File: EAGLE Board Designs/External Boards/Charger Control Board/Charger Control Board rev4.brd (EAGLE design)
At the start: 81 parts

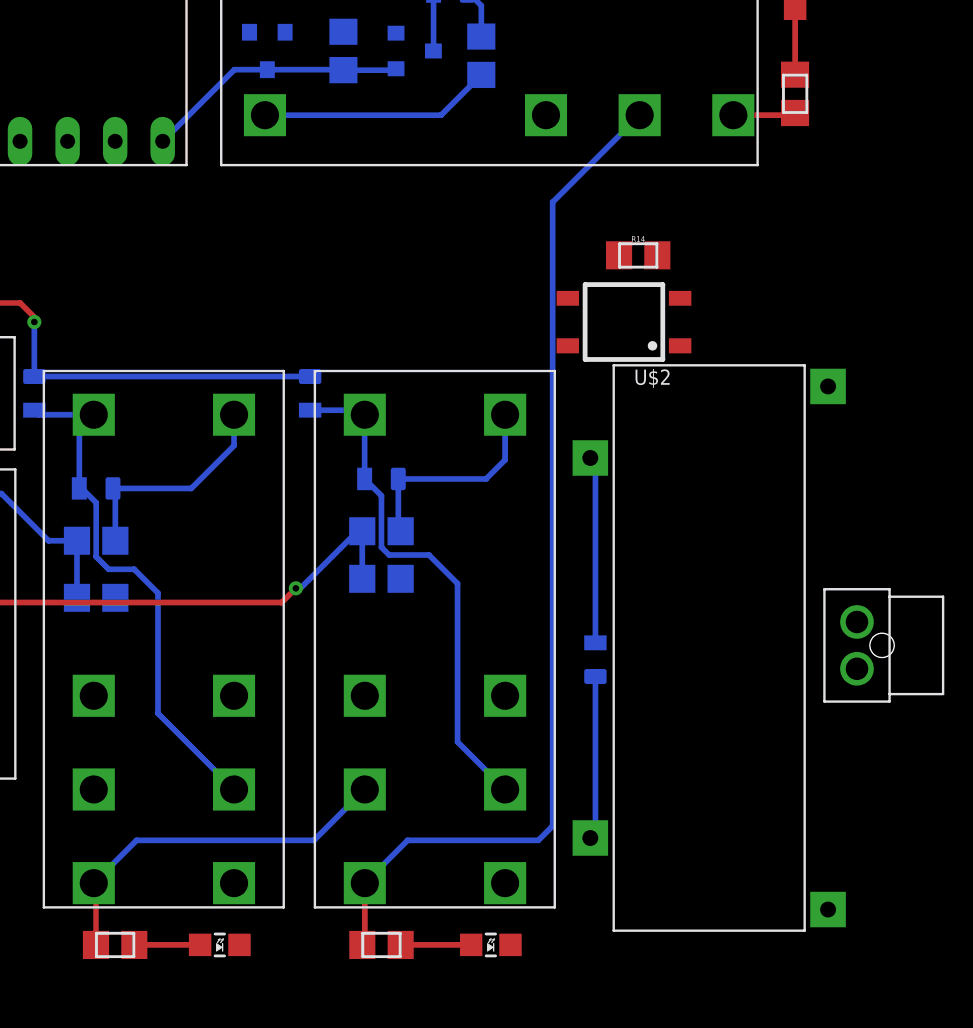
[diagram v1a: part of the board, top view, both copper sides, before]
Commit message: Routed charger
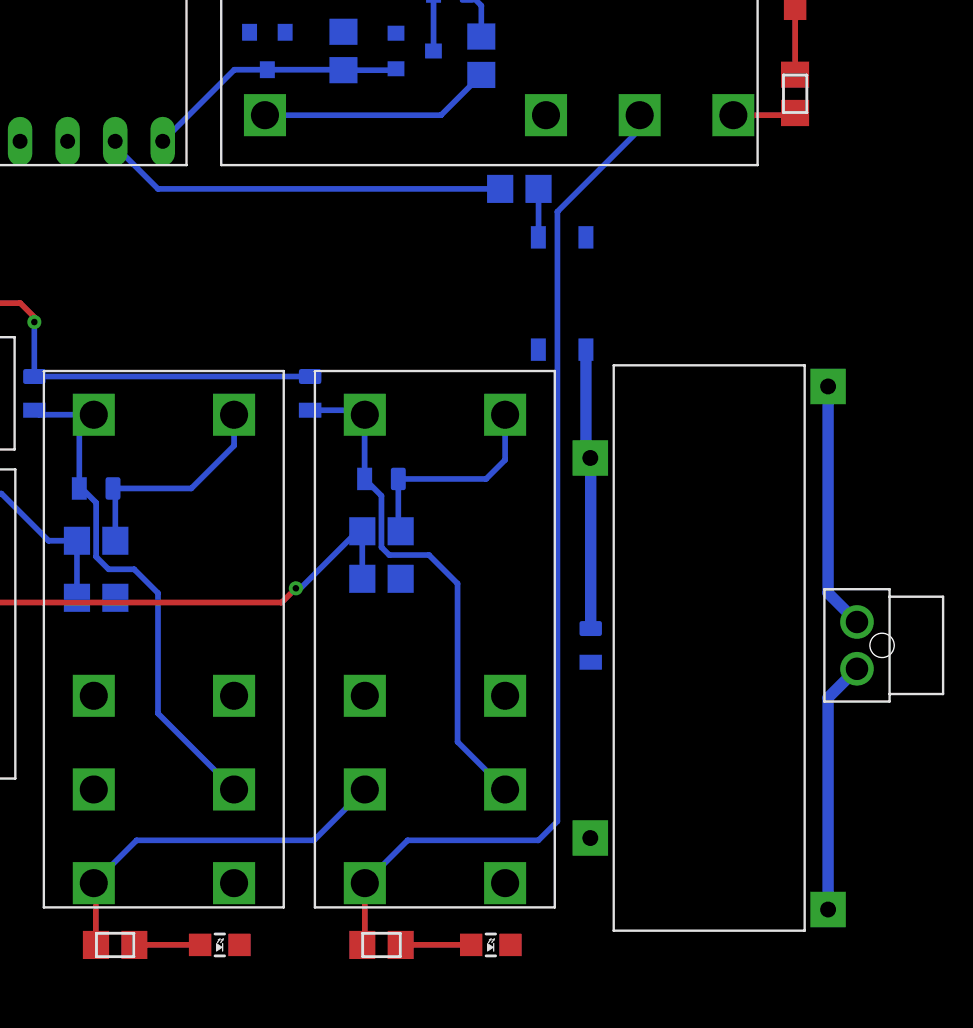
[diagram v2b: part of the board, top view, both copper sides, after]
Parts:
- moved R14 7.28 mm to (-24.1, 63.2), flipped to the bottom, turned to 180 degrees
- moved U$2 3.64 mm to (-21.8, 57.7), flipped to the bottom, turned to 180 degrees
- moved D3 0.80 mm to (-20.3, 38.9), turned to 90 degrees
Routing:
- net TOGGLE_CHARGER: track 0.00 -> 21.8 mm
- net CHARGER_1: track 0.00 -> 13.4 mm
- net CHARGER_2: track 0.00 -> 13.1 mm
- net GND: track 9.60 -> 0.00 mm
- net CHARGE_CONTROL: track 8.35 -> 15.1 mm
- net N$10: track 0.00 -> 2.59 mm
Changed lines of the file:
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@@
 <attribute name="VALUE" x="-36.0172" y="52.324" size="0.3048" layer="28" rot="MR90" align="top-center"/>
 </element>
-<element name="D3" library="HyTechDevices" package="0805_D" value="DIODE" x="-20.066" y="38.1" smashed="yes" rot="MR270">
-<attribute name="NAME" x="-20.7899" y="38.1" size="0.3048" layer="26" rot="MR270" align="bottom-center"/>
-<attribute name="VALUE" x="-19.3548" y="38.1" size="0.3048" layer="28" rot="MR270" align="top-center"/>
+<element name="D3" library="HyTechDevices" package="0805_D" value="DIODE" x="-20.32" y="38.862" smashed="yes" rot="MR90">
+<attribute name="NAME" x="-19.5961" y="38.862" size="0.3048" layer="26" rot="MR90" align="bottom-center"/>
+<attribute name="VALUE" x="-21.0312" y="38.862" size="0.3048" layer="28" rot="MR90" align="top-center"/>
 </element>
 <element name="D6" library="HyTechDevices" package="0805_D" value="TS4148 RYG" x="-31.496" y="47.752" smashed="yes" rot="MR180">
@@
 <attribute name="VALUE" x="-65.786" y="50.3428" size="0.3048" layer="27" align="top-center"/>
 </element>
-<element name="R14" library="HyTechDevices" package="0805" value="360" x="-17.78" y="59.69" smashed="yes">
-<attribute name="NAME" x="-17.78" y="60.4139" size="0.3048" layer="25" align="bottom-center"/>
-<attribute name="TOLERANCE" value="1%" x="-17.78" y="59.69" size="1.778" layer="27" display="off"/>
-<attribute name="VALUE" x="-17.78" y="58.9788" size="0.3048" layer="27" align="top-center"/>
+<element name="R14" library="HyTechDevices" package="0805" value="360" x="-24.13" y="63.246" smashed="yes" rot="MR180">
+<attribute name="NAME" x="-24.13" y="62.5221" size="0.3048" layer="26" rot="MR180" align="bottom-center"/>
+<attribute name="TOLERANCE" value="1%" x="-24.13" y="63.246" size="1.778" layer="28" rot="MR180" display="off"/>
+<attribute name="VALUE" x="-24.13" y="63.9572" size="0.3048" layer="28" rot="MR180" align="top-center"/>
 </element>
 <element name="R15" library="HyTechDevices" package="0805" value="68" x="71.12" y="69.85" smashed="yes" rot="R90">
@@
 <attribute name="VALUE" x="-75.311" y="57.531" size="0.3048" layer="28" rot="MR0" align="bottom-center"/>
 </element>
-<element name="U$2" library="HyTechDevices" package="SOP04" value="CPC1002N" x="-18.542" y="56.134" smashed="yes" rot="R90">
-<attribute name="NAME" x="-16.002" y="53.594" size="0.8128" layer="25" rot="R180"/>
-<attribute name="VALUE" x="-16.002" y="59.944" size="1.27" layer="27" rot="R180"/>
+<element name="U$2" library="HyTechDevices" package="SOP04" value="CPC1002N" x="-21.844" y="57.658" smashed="yes" rot="MR180">
+<attribute name="NAME" x="-24.384" y="60.198" size="0.8128" layer="26" rot="MR270"/>
+<attribute name="VALUE" x="-18.034" y="60.198" size="1.27" layer="28" rot="MR270"/>
 </element>
 <element name="U$4" library="HyTechDevices" package="TEENSY_3.2_SIMPLE" value="TEENSY_3.2_SIMPLE" x="-41.91" y="64.516" smashed="yes" rot="R90"/>
@@
 <contactref element="R29" pad="2"/>
 <contactref element="R31" pad="2"/>
-<wire x1="-20.066" y1="39" x2="-20.066" y2="48.598" width="0.3048" layer="16"/>
 <contactref element="U$3" pad="C1"/>
 <wire x1="68.58" y1="78.52" x2="78.74" y2="78.52" width="0" layer="19" extent="1-1"/>
@@
 <wire x1="54.61" y1="68.335" x2="59.69" y2="68.335" width="0" layer="19" extent="1-1"/>
 <wire x1="-9.398" y1="74.964" x2="54.61" y2="68.335" width="0" layer="19" extent="1-1"/>
-<wire x1="-15.542" y1="57.404" x2="-9.398" y2="74.964" width="0" layer="19" extent="1-1"/>
-<wire x1="-20.066" y1="48.598" x2="-15.542" y2="57.404" width="0" layer="19" extent="1-16"/>
-<wire x1="-20.34" y1="28.572" x2="-20.066" y2="39" width="0" layer="19" extent="16-16"/>
+<wire x1="-20.574" y1="60.658" x2="-9.398" y2="74.964" width="0" layer="19" extent="1-1"/>
+<wire x1="-20.32" y1="37.962" x2="-20.574" y2="60.658" width="0" layer="19" extent="1-16"/>
+<wire x1="-20.32" y1="37.962" x2="-20.34" y2="28.572" width="0" layer="19" extent="16-16"/>
 <wire x1="-24.892" y1="26.162" x2="-20.34" y2="28.572" width="0" layer="19" extent="1-1"/>
 <wire x1="-24.604" y1="22.86" x2="-24.892" y2="26.162" width="0" layer="19" extent="1-1"/>
-<wire x1="-30.471" y1="42.418" x2="-20.066" y2="39" width="0" layer="19" extent="16-16"/>
+<wire x1="-30.471" y1="42.418" x2="-20.32" y2="37.962" width="0" layer="19" extent="16-16"/>
 <wire x1="-39.082" y1="22.86" x2="-24.604" y2="22.86" width="0" layer="19" extent="1-1"/>
 <wire x1="-39.37" y1="26.162" x2="-39.082" y2="22.86" width="0" layer="19" extent="1-1"/>
@@
 <contactref element="U$2" pad="1"/>
 <contactref element="R14" pad="2"/>
-<wire x1="-15.542" y1="54.864" x2="-16.755" y2="59.69" width="0" layer="19" extent="1-1"/>
+<wire x1="-23.105" y1="63.246" x2="-23.105" y2="60.667" width="0.3048" layer="16"/>
+<wire x1="-23.105" y1="60.667" x2="-23.114" y2="60.658" width="0.3048" layer="16"/>
 </signal>
 <signal name="TOGGLE_CHARGER">
 <contactref element="R14" pad="1"/>
 <contactref element="U$4" pad="D11"/>
-<wire x1="-45.72" y1="65.786" x2="-18.805" y2="59.69" width="0" layer="19" extent="1-1"/>
+<wire x1="-25.155" y1="63.246" x2="-43.434" y2="63.246" width="0.3048" layer="16"/>
+<wire x1="-43.434" y1="63.246" x2="-45.72" y2="65.532" width="0.3048" layer="16"/>
+<wire x1="-45.72" y1="65.532" x2="-45.72" y2="65.786" width="0.3048" layer="16"/>
 </signal>
 <signal name="CHARGE_CONTROL">
 <contactref element="U$2" pad="3"/>
 <contactref element="D3" pad="C"/>
-<wire x1="-20.066" y1="37.2" x2="-20.066" y2="28.846" width="0.3048" layer="16"/>
 <contactref element="U$3" pad="C2"/>
-<wire x1="-20.34" y1="48.872" x2="-21.542" y2="57.404" width="0" layer="19" extent="1-1"/>
-<wire x1="-20.066" y1="37.2" x2="-20.34" y2="48.872" width="0" layer="19" extent="16-16"/>
+<wire x1="-20.32" y1="39.762" x2="-20.34" y2="39.782" width="0.3048" layer="16"/>
+<wire x1="-20.405" y1="48.937" x2="-20.34" y2="48.872" width="0.3048" layer="16"/>
+<wire x1="-20.574" y1="54.658" x2="-20.574" y2="49.106" width="0.6096" layer="16"/>
+<wire x1="-20.574" y1="49.106" x2="-20.405" y2="48.937" width="0.6096" layer="16"/>
+<wire x1="-20.32" y1="39.762" x2="-20.32" y2="48.852" width="0.6096" layer="16"/>
+<wire x1="-20.32" y1="48.852" x2="-20.405" y2="48.937" width="0.6096" layer="16"/>
 </signal>
 <signal name="+5V">
@@
 <wire x1="-26.162" y1="73.036" x2="-26.162" y2="71.383" width="0.3048" layer="16"/>
 <wire x1="-26.913" y1="73.787" x2="-10.16" y2="136.915" width="0" layer="19" extent="1-16"/>
-<wire x1="-60.452" y1="42.672" x2="-26.162" y2="71.383" width="0" layer="19" extent="1-16"/>
-<wire x1="-21.542" y1="54.864" x2="-26.162" y2="71.383" width="0" layer="19" extent="1-16"/>
+<wire x1="-26.162" y1="71.383" x2="-60.452" y2="42.672" width="0" layer="19" extent="1-16"/>
+<wire x1="-23.114" y1="54.658" x2="-26.162" y2="71.383" width="0" layer="19" extent="1-16"/>
 </signal>
 <signal name="N$8">
@@
 <wire x1="-32.385" y1="26.162" x2="-32.385" y2="22.996" width="0.3048" layer="1"/>
 <wire x1="-32.385" y1="22.996" x2="-32.521" y2="22.86" width="0.3048" layer="1"/>
-<wire x1="-17.7038" y1="67.183" x2="-22.352" y2="62.5348" width="0.3048" layer="16"/>
-<wire x1="-22.352" y1="62.5348" x2="-22.352" y2="29.21" width="0.3048" layer="16"/>
-<wire x1="-23.114" y1="28.448" x2="-22.352" y2="29.21" width="0.3048" layer="16"/>
+<wire x1="-17.7038" y1="67.183" x2="-17.7038" y2="66.421" width="0.3048" layer="16"/>
+<wire x1="-17.7038" y1="66.421" x2="-22.098" y2="62.0268" width="0.3048" layer="16"/>
+<wire x1="-22.098" y1="62.0268" x2="-22.098" y2="29.464" width="0.3048" layer="16"/>
+<wire x1="-22.098" y1="29.464" x2="-23.114" y2="28.448" width="0.3048" layer="16"/>
 <wire x1="-32.385" y1="26.162" x2="-30.099" y2="28.448" width="0.3048" layer="16"/>
 <wire x1="-30.099" y1="28.448" x2="-23.114" y2="28.448" width="0.3048" layer="16"/>
-<wire x1="-17.7038" y1="67.183" x2="20.32" y2="134.99" width="0" layer="19" extent="1-1"/>
+<wire x1="-17.7038" y1="66.421" x2="20.32" y2="134.99" width="0" layer="19" extent="1-1"/>
 </signal>
 <signal name="N$5">
@@
 <contactref element="U$3" pad="S2"/>
 <contactref element="CHARGER" pad="P$2"/>
-<wire x1="-6.096" y1="40.112" x2="-7.64" y2="52.692" width="0" layer="19" extent="1-1"/>
+<wire x1="-7.64" y1="52.692" x2="-7.64" y2="41.656" width="0.6096" layer="16"/>
+<wire x1="-7.64" y1="41.656" x2="-6.19456875" y2="40.21056875" width="0.6096" layer="16"/>
+<wire x1="-6.19456875" y1="40.21056875" x2="-6.096" y2="40.112" width="0" layer="19" extent="16-16"/>
 </signal>
 <signal name="CHARGER_1">
 <contactref element="U$3" pad="S1"/>
 <contactref element="CHARGER" pad="P$1"/>
-<wire x1="-7.64" y1="24.752" x2="-6.096" y2="37.612" width="0" layer="19" extent="1-1"/>
+<wire x1="-7.64" y1="24.752" x2="-7.64" y2="36.068" width="0.6096" layer="16"/>
+<wire x1="-7.64" y1="36.068" x2="-6.19456875" y2="37.51343125" width="0.6096" layer="16"/>
+<wire x1="-6.19456875" y1="37.51343125" x2="-6.096" y2="37.612" width="0" layer="19" extent="16-16"/>
 </signal>
 <signal name="N$4">

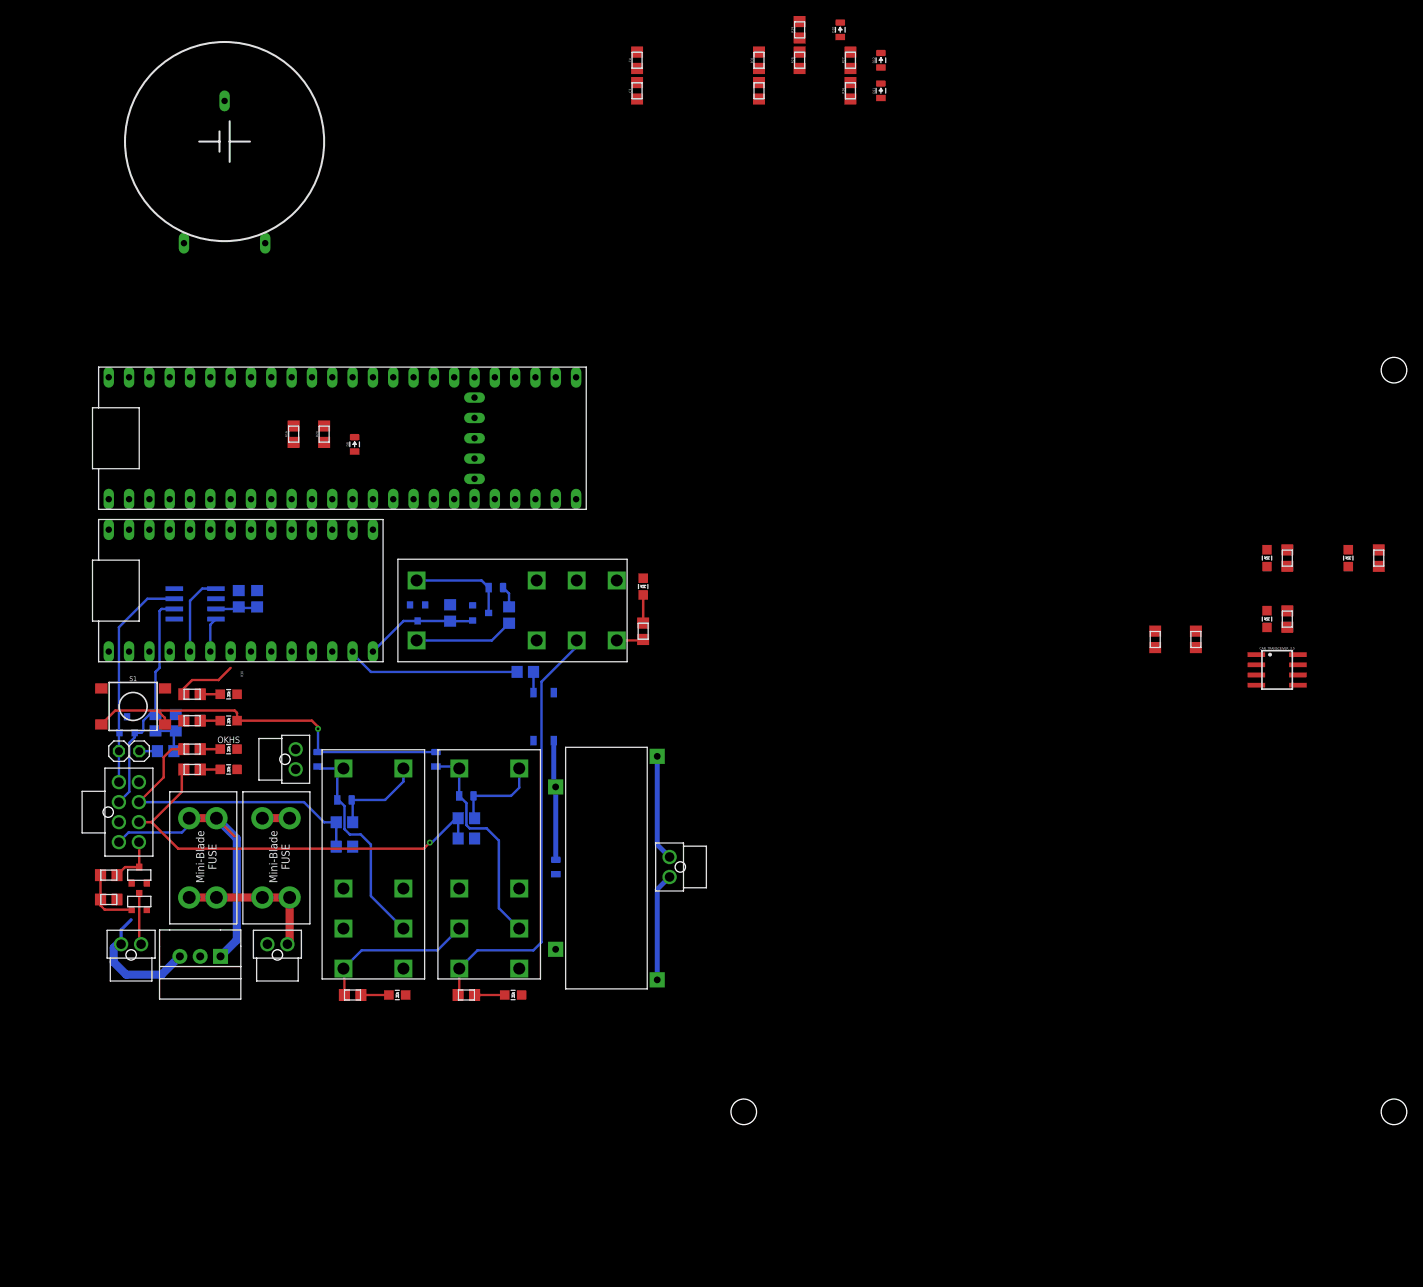
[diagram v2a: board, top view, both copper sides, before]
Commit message: Routed teensy read shutdown
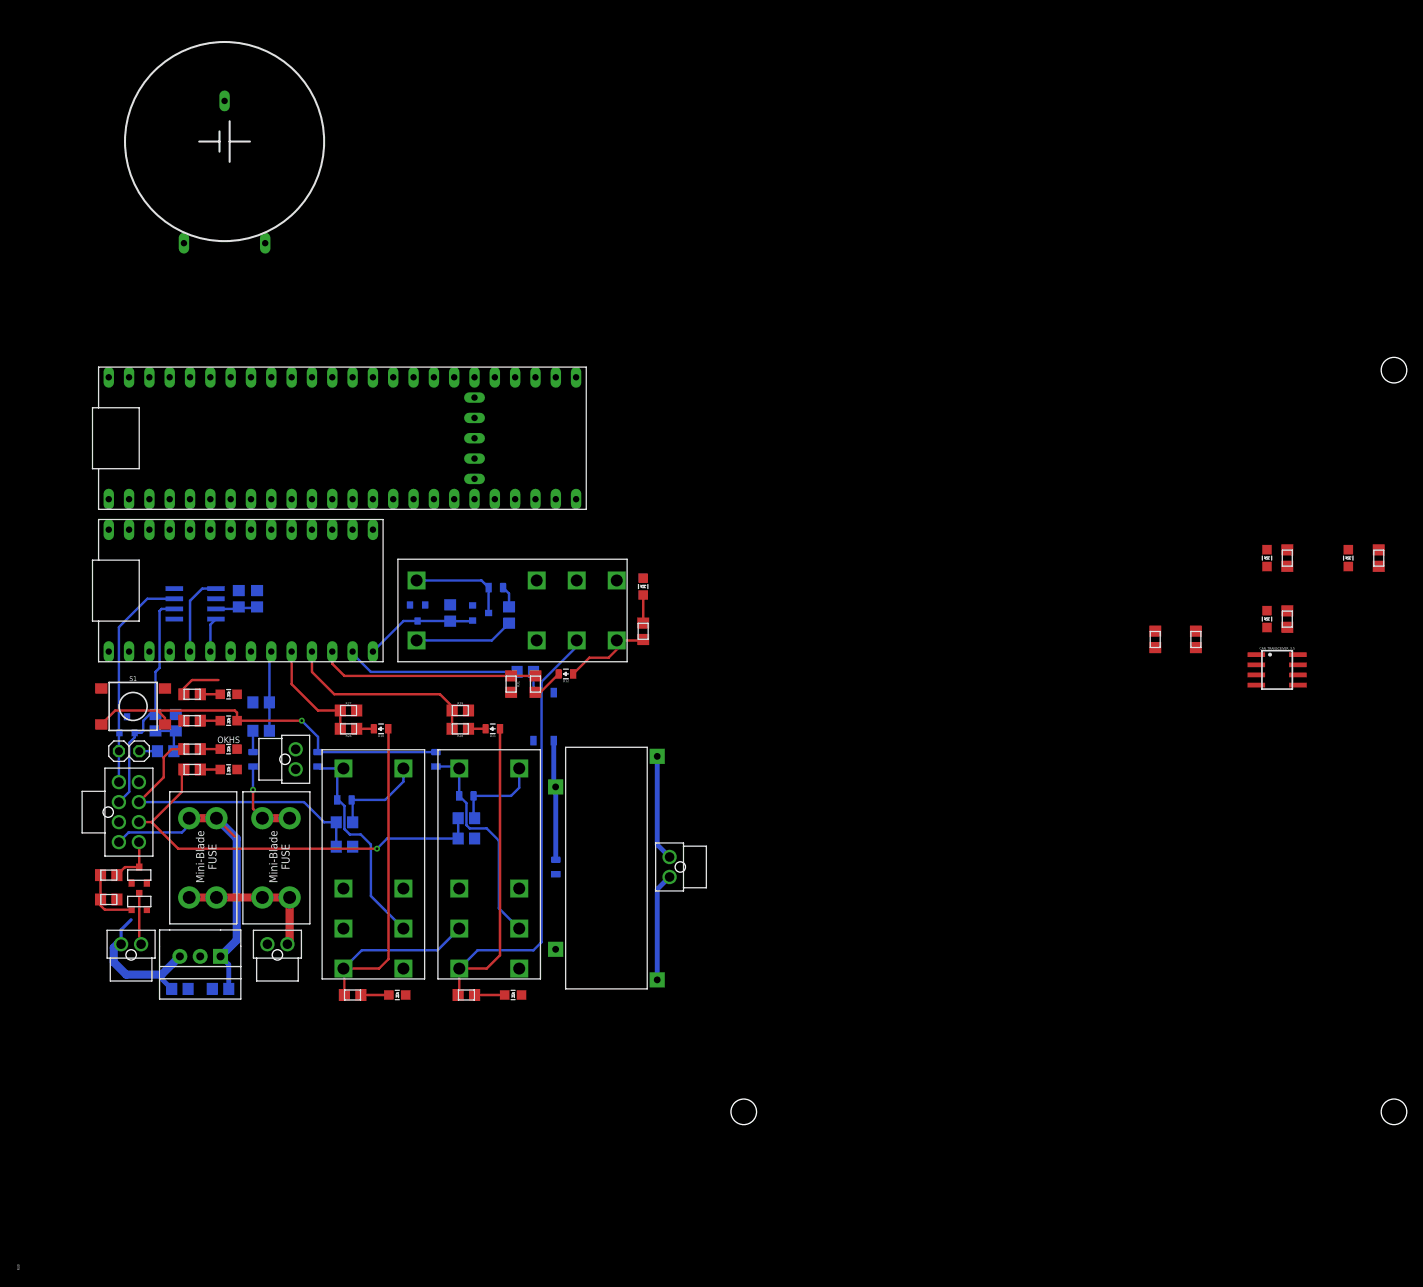
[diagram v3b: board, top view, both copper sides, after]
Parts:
- moved C4 129.4 mm to (-67.3, 23.6), flipped to the bottom, turned to 0 degrees
- moved C3 123.8 mm to (-62.2, 23.6), flipped to the bottom, turned to 180 degrees
- moved D10 104.5 mm to (-42.2, 56.1), turned to 180 degrees
- moved R27 102.7 mm to (-46.2, 58.4), turned to 0 degrees
- moved R26 101.5 mm to (-46.2, 56.1), turned to 180 degrees
- moved R29 95.1 mm to (-32.3, 58.4), turned to 0 degrees
- moved R28 93.7 mm to (-32.3, 56.1), turned to 180 degrees
- moved D11 93.4 mm to (-28.2, 56.1), turned to 180 degrees
- moved D12 86.2 mm to (-19.1, 63.0), turned to 180 degrees
- moved R31 83.9 mm to (-25.9, 61.7), turned to 270 degrees
- moved R30 79.3 mm to (-22.9, 61.7)
- moved D8 41.4 mm to (-58.2, 52.3), flipped to the bottom
- moved R19 37.3 mm to (-57.1, 55.9), flipped to the bottom, turned to 180 degrees
- moved R20 34.4 mm to (-57.1, 59.4), flipped to the bottom, turned to 0 degrees
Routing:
- net SHUTDOWN_B: track 19.9 -> 54.8 mm
- net SHUTDOWN_C: track 54.6 -> 88.6 mm
- net SHUTDOWN_D_READ: track 0.00 -> 27.6 mm
- net SHUTDOWN_C_READ: track 0.00 -> 24.6 mm
- net SHUTDOWN_B_READ: track 0.00 -> 13.8 mm
- net SHUTDOWN_A_READ: track 0.00 -> 10.0 mm
- net SHUTDOWN_D: track 3.35 -> 11.3 mm
- net SHUTDOWN_A: track 3.40 -> 10.4 mm, vias 0 -> 1
- net +12V: track 39.0 -> 43.5 mm
- net N$21: track 0.00 -> 3.86 mm
- net N$14: track 0.00 -> 2.66 mm
- net +5V: track 21.6 -> 23.9 mm
- net SOFTWARE_SHUTDOWN: track 21.7 -> 19.6 mm
- net N$18: track 0.00 -> 2.14 mm
- net N$20: track 0.00 -> 2.14 mm
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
